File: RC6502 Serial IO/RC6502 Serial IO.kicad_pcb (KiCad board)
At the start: 2 copper layers, 99.1 x 66 mm, 16 parts, among them J1 CONN_01X39, J2 Arduino Nano, J3 SPI Breakout, SW1 Reset, U1 74HCT04, U2 WD65C21, U3 74LS138, U4 MCP23S17

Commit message: Exported files
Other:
- board text added: "Address A0 - A15"
- board text added: "Data D7 - D0"
- board text added: "GND"
- board text added: "Phi 2"
- board text added: "Pin 1"
- board text added: "RC6502 Serial IO Revision A"
- board text added: "Reset"
- board text added: "VCC"
- board text added: "WR"
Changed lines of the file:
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@@
     (area 97.085 66.335 203.675001 143.975001)
     (thickness 1.6)
-    (drawings 11)
+    (drawings 38)
     (tracks 529)
     (zones 0)
@@
     (visible_elements 7FFFFFFF)
     (pcbplotparams
-      (layerselection 0x00030_80000001)
+      (layerselection 0x011fc_80000001)
       (usegerberextensions false)
       (excludeedgelayer true)
@@
       (padsonsilk false)
       (subtractmaskfromsilk false)
-      (outputformat 1)
+      (outputformat 4)
       (mirror false)
-      (drillshape 1)
+      (drillshape 0)
       (scaleselection 1)
-      (outputdirectory ""))
+      (outputdirectory "D:/ownCloud/Documents/Projects/RC6502/RC6502 Serial IO/export/"))
   )
   (net 0 "")
@@
     )
   )
+  (gr_text "RC6502 Serial IO\nRevision A" (at 147.32 72.39) (layer F.SilkS)
+    (effects (font (size 1.5 1.5) (thickness 0.3)) (justify left))
+  )
+  (gr_text "Address A0 - A15" (at 177.8 130.81) (layer F.SilkS)
+    (effects (font (size 1.5 1.5) (thickness 0.3)))
+  )
+  (gr_text "Data\nD7 - D0" (at 121.92 128.27) (layer F.SilkS)
+    (effects (font (size 1.5 1.5) (thickness 0.3)))
+  )
+  (gr_text GND (at 156.21 125.73 270) (layer F.SilkS)
+    (effects (font (size 1.5 1.5) (thickness 0.3)) (justify left))
+  )
+  (gr_text VCC (at 153.67 125.73 270) (layer F.SilkS)
+    (effects (font (size 1.5 1.5) (thickness 0.3)) (justify left))
+  )
+  (gr_text "Phi 2" (at 151.13 125.73 270) (layer F.SilkS)
+    (effects (font (size 1.5 1.5) (thickness 0.3)) (justify left))
+  )
+  (gr_text WR (at 138.43 125.73 270) (layer F.SilkS)
+    (effects (font (size 1.5 1.5) (thickness 0.3)) (justify left))
+  )
+  (gr_line (start 157.48 128.27) (end 195.58 128.27) (angle 90) (layer F.SilkS) (width 0.2))
+  (gr_line (start 157.48 124.46) (end 157.48 134.62) (angle 90) (layer F.SilkS) (width 0.2))
+  (gr_line (start 154.94 124.46) (end 157.48 124.46) (angle 90) (layer F.SilkS) (width 0.2))
+  (gr_line (start 154.94 124.46) (end 154.94 134.62) (angle 90) (layer F.SilkS) (width 0.2))
+  (gr_line (start 152.4 124.46) (end 154.94 124.46) (angle 90) (layer F.SilkS) (width 0.2))
+  (gr_line (start 152.4 124.46) (end 152.4 134.62) (angle 90) (layer F.SilkS) (width 0.2))
+  (gr_line (start 149.86 124.46) (end 152.4 124.46) (angle 90) (layer F.SilkS) (width 0.2))
+  (gr_line (start 147.32 124.46) (end 147.32 134.62) (angle 90) (layer F.SilkS) (width 0.2))
+  (gr_text Reset (at 148.59 125.73 270) (layer F.SilkS)
+    (effects (font (size 1.5 1.5) (thickness 0.3)) (justify left))
+  )
+  (gr_line (start 149.86 124.46) (end 149.86 134.62) (angle 90) (layer F.SilkS) (width 0.2))
+  (gr_line (start 147.32 124.46) (end 149.86 124.46) (angle 90) (layer F.SilkS) (width 0.2))
+  (gr_line (start 139.7 124.46) (end 139.7 134.62) (angle 90) (layer F.SilkS) (width 0.2))
+  (gr_line (start 137.16 124.46) (end 139.7 124.46) (angle 90) (layer F.SilkS) (width 0.2))
+  (gr_line (start 137.16 134.62) (end 137.16 124.46) (angle 90) (layer F.SilkS) (width 0.2))
+  (gr_line (start 132.08 124.46) (end 132.08 134.62) (angle 90) (layer F.SilkS) (width 0.2))
+  (gr_line (start 111.76 124.46) (end 132.08 124.46) (angle 90) (layer F.SilkS) (width 0.2))
+  (gr_line (start 111.76 134.62) (end 111.76 124.46) (angle 90) (layer F.SilkS) (width 0.2))
+  (gr_text "Pin 1" (at 196.85 123.19 270) (layer F.SilkS)
+    (effects (font (size 1.5 1.5) (thickness 0.3)) (justify left))
+  )
+  (gr_line (start 195.58 121.92) (end 198.12 121.92) (angle 90) (layer F.SilkS) (width 0.2))
+  (gr_line (start 195.58 134.62) (end 195.58 121.92) (angle 90) (layer F.SilkS) (width 0.2))
   (gr_line (start 193.04 99.06) (end 198.12 99.06) (angle 90) (layer F.SilkS) (width 0.2))
   (gr_line (start 193.04 111.76) (end 193.04 99.06) (angle 90) (layer F.SilkS) (width 0.2))

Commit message: Serial IO Revision B
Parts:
- added C5: 10nF, Capacitors_THT:C_Disc_D4.7mm_W2.5mm_P5.00mm, F.Cu at (149.2, 115.6)
- added D1: 1N4848, Diodes_THT:D_DO-35_SOD27_P7.62mm_Horizontal, F.Cu at (160.0, 88.9)
- added J4: Peripheral Bus, Connectors:IDC_Header_Straight_40pins, F.Cu at (106.7, 124.5)
- added R4: 10k, Resistors_THT:R_Axial_DIN0207_L6.3mm_D2.5mm_P10.16mm_Horizontal, F.Cu at (166.4, 81.3)
- added R5: 10k, Resistors_THT:R_Axial_DIN0207_L6.3mm_D2.5mm_P10.16mm_Horizontal, F.Cu at (189.2, 81.3)
- C4: value 10nF -> 100nF
- J3: footprint Pin_Headers:Pin_Header_Straight_1x05_Pitch2.54mm -> Pin_Headers:Pin_Header_Angled_1x06_Pitch2.54mm
- U3: value 74LS138 -> 74HCT38
- moved R3 74.4 mm to (179.1, 85.1)
- moved R2 61.3 mm to (179.1, 88.9)
- moved U2 53.2 mm to (115.6, 72.4), turned to 0 degrees
- moved C4 38.2 mm to (145.4, 115.6), turned to 270 degrees
- moved C2 36.4 mm to (141.6, 115.6), turned to 270 degrees
- moved R1 35.9 mm to (166.4, 88.9)
- moved C1 34.3 mm to (156.2, 107.3), turned to 0 degrees
- moved C3 18.0 mm to (178.4, 107.3), turned to 0 degrees
- moved U1 15.6 mm to (156.2, 120.0)
- moved J3 14.6 mm to (196.8, 95.9), turned to 0 degrees
- moved U3 11.1 mm to (178.4, 120.0)
- moved U4 10.2 mm to (141.6, 72.4), turned to 0 degrees
- moved JP1 2.54 mm to (185.4, 73.7)
- moved J2 1.27 mm to (161.3, 92.7)
- moved SW1 0.90 mm to (189.9, 70.5)
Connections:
- net KBD_DA renamed KBD_STROBE
- net Net-(J2-Pad28) renamed P_RESET
- net OUT_READY renamed OUT_RDA
- net WR renamed RW
- C4 pad 1: OUT_DA -> VCC
- C4 pad 2: Net-(C4-Pad2) -> GND
- J1 pad 35: (no net) -> TX
- J1 pad 36: (no net) -> RX
- J2 pad 1: (no net) -> TX
- J2 pad 10: (no net) -> KBD_DETECT
- J2 pad 11: /CS1 -> (no net)
- J2 pad 12: /CS2 -> /CS1
- J2 pad 2: (no net) -> RX
- J2 pad 9: (no net) -> OUT_DETECT
- J3 pad 2: /CS2 -> /SCK
- J3 pad 3: /SCK -> /MOSI
- J3 pad 4: /MOSI -> /MISO
- J3 pad 5: /MISO -> GND
- JP1 pad 2: VCC -> Net-(D1-Pad2)
- R1 pad 1: VCC -> OUT_DETECT
- R1 pad 2: /CS1 -> VCC
- R2 pad 2: /CS2 -> /CS1
- U1 pad 2: Net-(C4-Pad2) -> Net-(C5-Pad2)
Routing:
- net GND: track 165.7 -> 0.00 mm, vias 2 -> 0
- net OUT_DETECT: track 0.00 -> 126.4 mm, vias 0 -> 2
- net KBD_DETECT: track 0.00 -> 99.1 mm, vias 0 -> 1
- net RX: track 0.00 -> 91.6 mm, vias 0 -> 3
- net Net-(C4-Pad2): track 90.4 -> 0.00 mm, vias 2 -> 0
- net /CS2: track 89.2 -> 0.00 mm, vias 2 -> 0
- net TX: track 0.00 -> 88.8 mm, vias 0 -> 2
- net /SCK: track 151.9 -> 79.7 mm, vias 4 -> 2
- net /CS1: track 77.7 -> 13.5 mm, vias 2 -> 0
- net OUT_D6: track 35.3 -> 92.8 mm, vias 1 -> 4
- net KBD_STROBE: track 41.6 -> 98.2 mm, vias 3 -> 4
- net OUT_D5: track 30.3 -> 86.4 mm, vias 1 -> 4
- net P_RESET: track 102.9 -> 158.6 mm, vias 4 -> 6
- net OUT_D4: track 25.2 -> 80.1 mm, vias 1 -> 4
- net OUT_D3: track 20.1 -> 73.7 mm, vias 1 -> 4
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- removed copper zone on F.Cu, net VCC
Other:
- board text added: "RC6502 Serial IO Revision B"
- board text added: "RW"
- board text added: "RX"
- board text added: "TX"
- board text removed: "RC6502 Serial IO Revision A"
- board text removed: "WR"

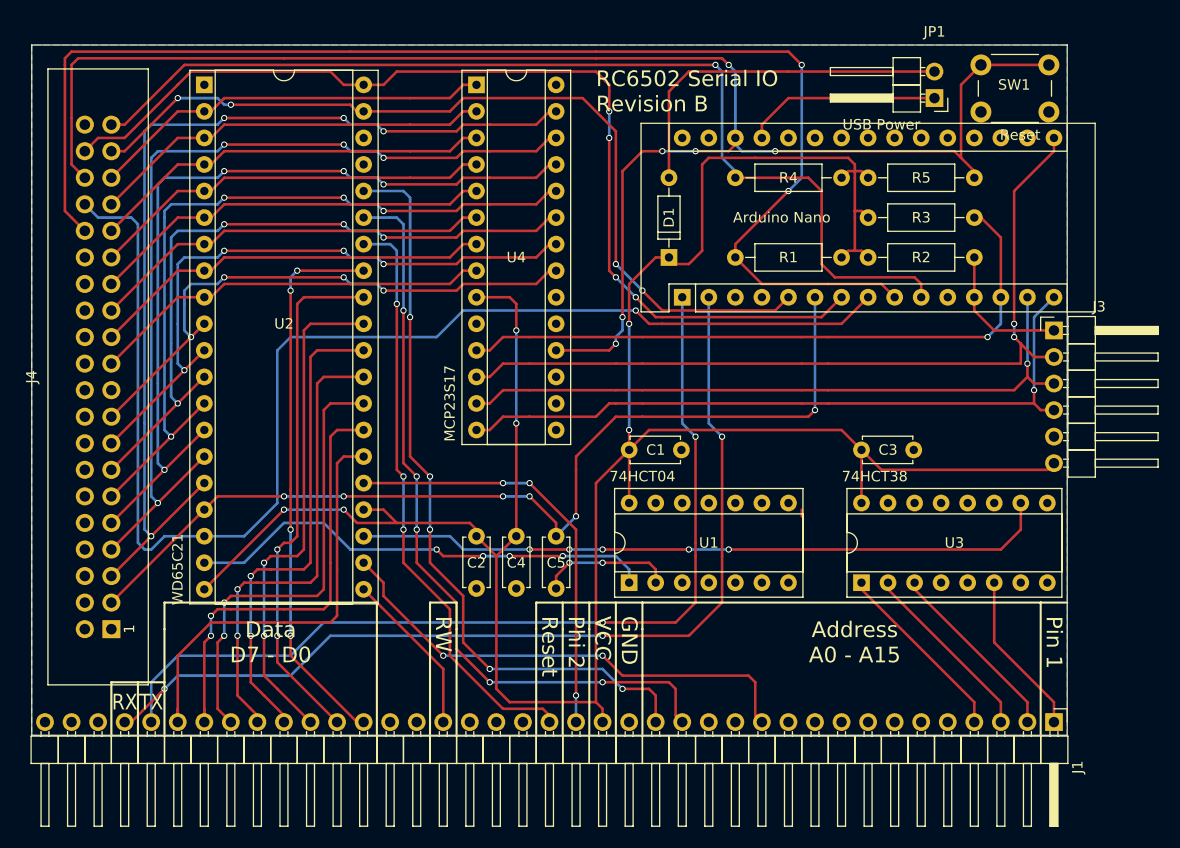
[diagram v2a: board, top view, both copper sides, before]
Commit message: Added SPI breakout details to silkscreen
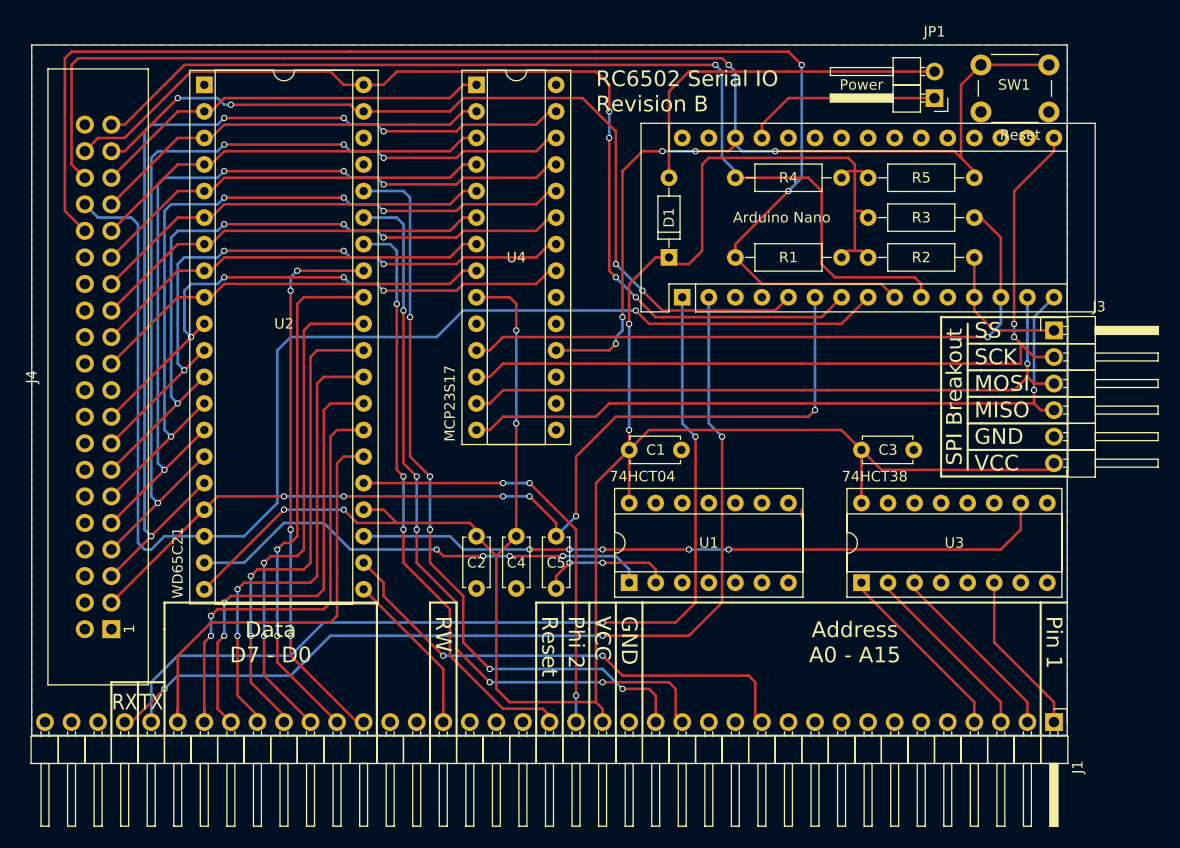
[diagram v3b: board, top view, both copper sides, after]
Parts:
- JP1: value USB Power -> Power
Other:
- board text added: "MISO"
- board text added: "MOSI"
- board text added: "SCK"
- board text added: "SPI Breakout"
- board text added: "SS"
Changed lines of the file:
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@@
     (links 122)
     (no_connects 0)
-    (area 99.009999 68.529999 198.170001 134.670001)
+    (area 97.085 66.335 208.915953 143.975001)
     (thickness 1.6)
-    (drawings 42)
+    (drawings 64)
     (tracks 796)
     (zones 0)
@@
   (page A4)
   (layers
-    (0 F.Cu signal hide)
-    (31 B.Cu signal hide)
+    (0 F.Cu signal)
+    (31 B.Cu signal)
     (32 B.Adhes user)
     (33 F.Adhes user)
@@
     (pcbplotparams
       (layerselection 0x011fc_80000001)
-      (usegerberextensions false)
+      (usegerberextensions true)
       (excludeedgelayer true)
       (linewidth 0.100000)
@@
       (padsonsilk false)
       (subtractmaskfromsilk false)
-      (outputformat 4)
+      (outputformat 1)
       (mirror false)
       (drillshape 0)
@@
       (effects (font (size 1 1) (thickness 0.15)))
     )
-    (fp_text value "USB Power" (at 5.08 -2.54 180) (layer F.SilkS)
+    (fp_text value Power (at 6.985 1.27 180) (layer F.SilkS)
       (effects (font (size 1 1) (thickness 0.15)))
     )
@@
       (effects (font (size 1 1) (thickness 0.15)))
     )
-    (fp_text value WD65C21 (at -2.54 46.355 270) (layer F.SilkS)
+    (fp_text value WD65C21 (at -2.54 45.72 270) (layer F.SilkS)
       (effects (font (size 1 1) (thickness 0.15)))
     )
@@
     )
   )
+  (gr_line (start 188.595 97.155) (end 189.865 97.155) (angle 90) (layer F.SilkS) (width 0.2))
+  (gr_line (start 188.595 99.695) (end 189.865 99.695) (angle 90) (layer F.SilkS) (width 0.2))
+  (gr_line (start 188.595 102.235) (end 189.865 102.235) (angle 90) (layer F.SilkS) (width 0.2))
+  (gr_line (start 188.595 104.775) (end 189.865 104.775) (angle 90) (layer F.SilkS) (width 0.2))
+  (gr_line (start 189.865 107.315) (end 188.595 107.315) (angle 90) (layer F.SilkS) (width 0.2))
+  (gr_line (start 189.865 107.315) (end 198.12 107.315) (angle 90) (layer F.SilkS) (width 0.2))
+  (gr_line (start 189.865 104.775) (end 198.12 104.775) (angle 90) (layer F.SilkS) (width 0.2))
+  (gr_line (start 189.865 102.235) (end 198.12 102.235) (angle 90) (layer F.SilkS) (width 0.2))
+  (gr_line (start 189.865 99.695) (end 198.12 99.695) (angle 90) (layer F.SilkS) (width 0.2))
+  (gr_line (start 189.865 97.155) (end 198.12 97.155) (angle 90) (layer F.SilkS) (width 0.2))
+  (gr_line (start 186.055 94.615) (end 198.12 94.615) (angle 90) (layer F.SilkS) (width 0.2))
+  (gr_line (start 198.12 109.855) (end 198.12 109.22) (angle 90) (layer F.SilkS) (width 0.2))
+  (gr_line (start 186.055 109.855) (end 198.12 109.855) (angle 90) (layer F.SilkS) (width 0.2))
+  (gr_line (start 186.055 109.855) (end 186.055 94.615) (angle 90) (layer F.SilkS) (width 0.2))
+  (gr_text "SPI Breakout" (at 187.325 102.235 90) (layer F.SilkS)
+    (effects (font (size 1.5 1.5) (thickness 0.3)))
+  )
+  (gr_line (start 188.595 109.22) (end 188.595 95.25) (angle 90) (layer F.SilkS) (width 0.2))
+  (gr_text SS (at 189.23 95.885) (layer F.SilkS)
+    (effects (font (size 1.5 1.5) (thickness 0.3)) (justify left))
+  )
+  (gr_text SCK (at 189.23 98.425) (layer F.SilkS)
+    (effects (font (size 1.5 1.5) (thickness 0.3)) (justify left))
+  )
+  (gr_text MOSI (at 189.23 100.965) (layer F.SilkS)
+    (effects (font (size 1.5 1.5) (thickness 0.3)) (justify left))
+  )
+  (gr_text MISO (at 189.23 103.505) (layer F.SilkS)
+    (effects (font (size 1.5 1.5) (thickness 0.3)) (justify left))
+  )
+  (gr_text GND (at 189.23 106.045) (layer F.SilkS)
+    (effects (font (size 1.5 1.5) (thickness 0.3)) (justify left))
+  )
+  (gr_text VCC (at 189.23 108.585) (layer F.SilkS)
+    (effects (font (size 1.5 1.5) (thickness 0.3)) (justify left))
+  )
   (gr_text RX (at 107.95 131.445) (layer F.SilkS)
     (effects (font (size 1.5 1.3) (thickness 0.2)))
@@
   (segment (start 145.415 93.345) (end 144.78 92.71) (width 0.25) (layer F.Cu) (net 1))
   (segment (start 141.605 92.71) (end 144.78 92.71) (width 0.25) (layer F.Cu) (net 1))
-  (segment (start 145.415 104.775) (end 145.415 115.57) (width 0.25) (layer F.Cu) (net 1) (status 800000))
+  (segment (start 145.415 104.775) (end 145.415 115.57) (width 0.25) (layer F.Cu) (net 1))
   (via (at 145.415 104.775) (size 0.6) (drill 0.4) (layers F.Cu B.Cu) (net 1))
   (segment (start 145.415 95.885) (end 145.415 104.775) (width 0.25) (layer B.Cu) (net 1))
